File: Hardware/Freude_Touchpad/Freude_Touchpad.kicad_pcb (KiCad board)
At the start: 4 copper layers, 26.4 x 26.4 mm, 9 parts, among them J1 Conn_01x06_Female, U1 IQS572

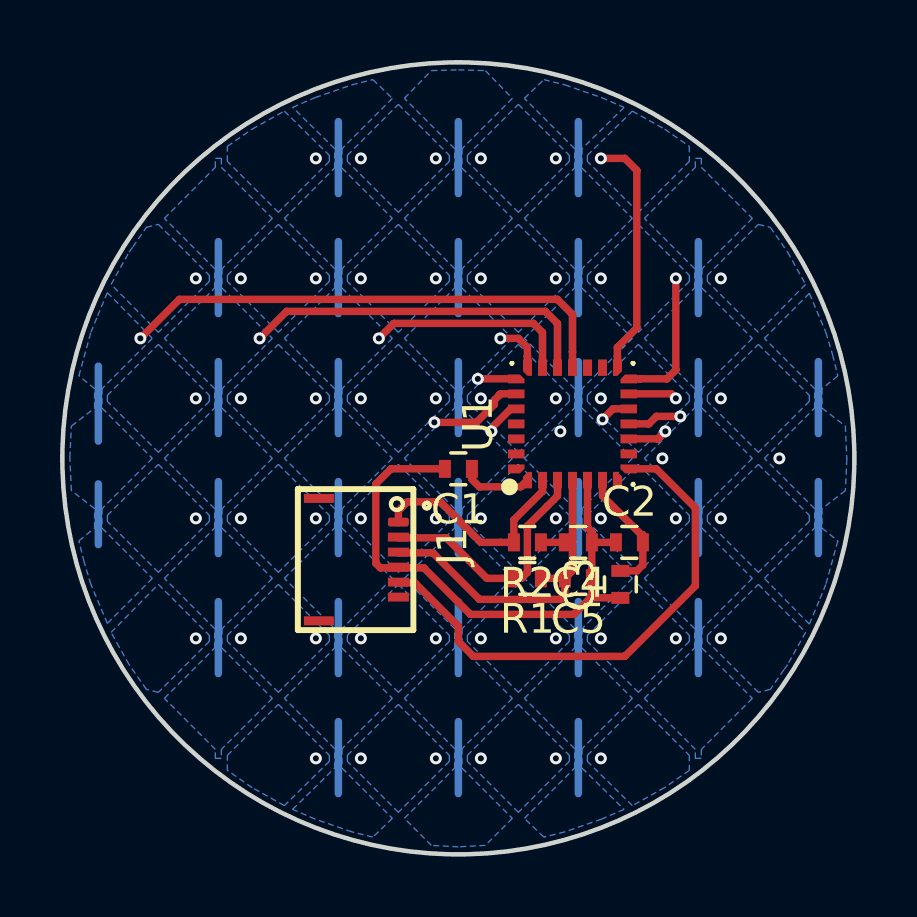
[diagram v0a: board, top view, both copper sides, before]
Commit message: broke PCB file into 3 folders and 3 PCB projects for each of the PCBAs, to make 3D drafting simpler. Created 3D housing project.
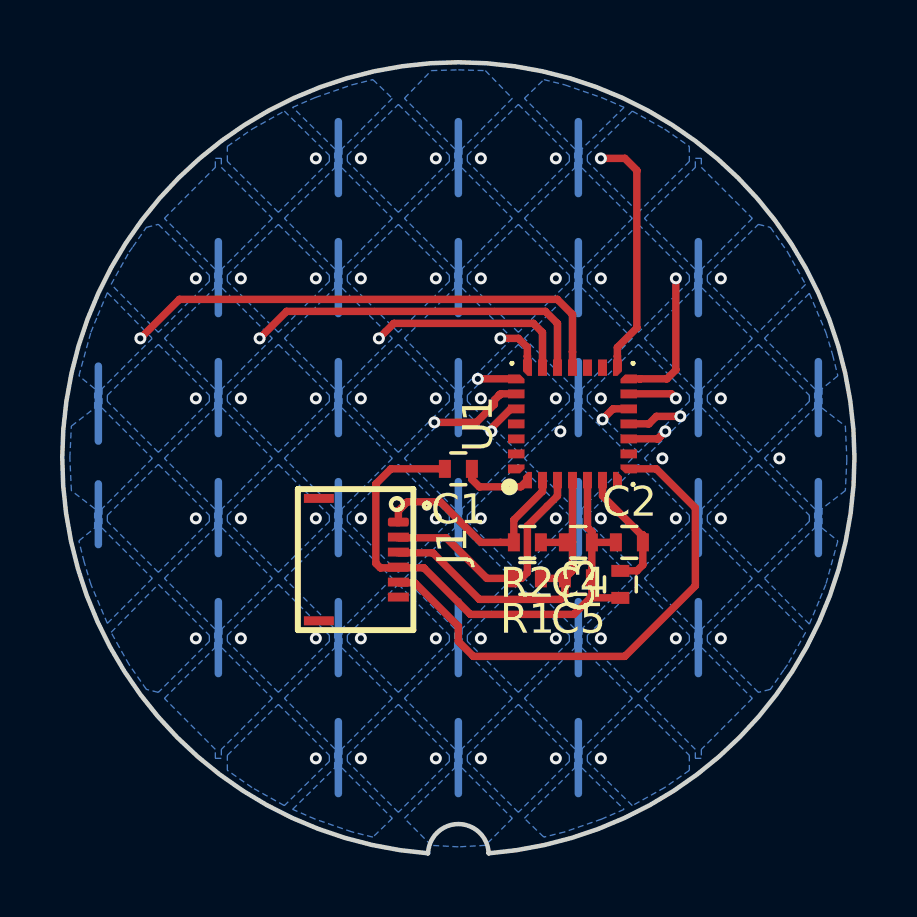
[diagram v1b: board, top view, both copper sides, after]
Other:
- outline, holes or cut-outs redrawn

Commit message: Changed location of connector to make routing of cable easier
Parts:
- moved J1 5.77 mm to (93.3, 100.0), turned to 90 degrees
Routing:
- net GNDA: track 19.1 -> 32.0 mm
- net /RDY_TP: track 17.5 -> 29.0 mm
- net +3.3VA: track 12.0 -> 21.8 mm
- net /SCL_TP: track 8.43 -> 17.6 mm
- net /SDA_TP: track 7.40 -> 11.9 mm
